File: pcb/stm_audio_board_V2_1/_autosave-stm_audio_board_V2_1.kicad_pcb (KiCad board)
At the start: 4 copper layers, 66.1 x 71 mm, 147 parts, among them J1 Power conn, J2 STlink, J3 Audio_sig, J4 Conn_01x01_taptempo, J5 Conn_01x10_display, J6 Conn_01x03_pot_ext, J7 Conn_01x8_pots_internal, SW1 SW_SPST, U1 STM32H747IGTx, U2 OP275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

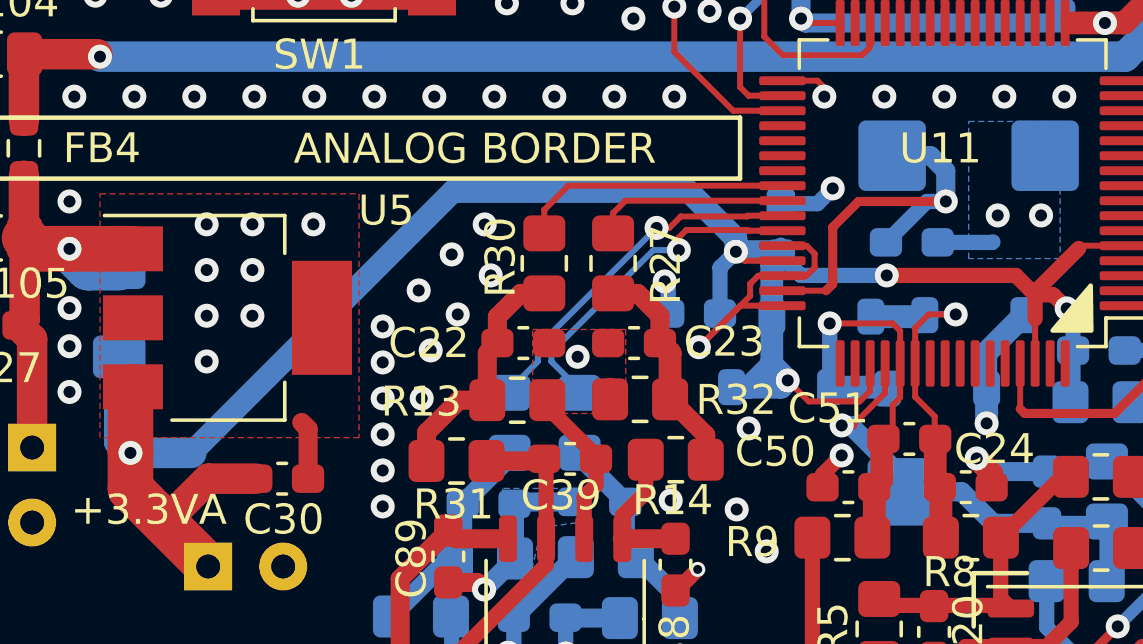
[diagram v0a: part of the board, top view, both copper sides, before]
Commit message: input stage is done, fixes for the audioboardV2_1 over
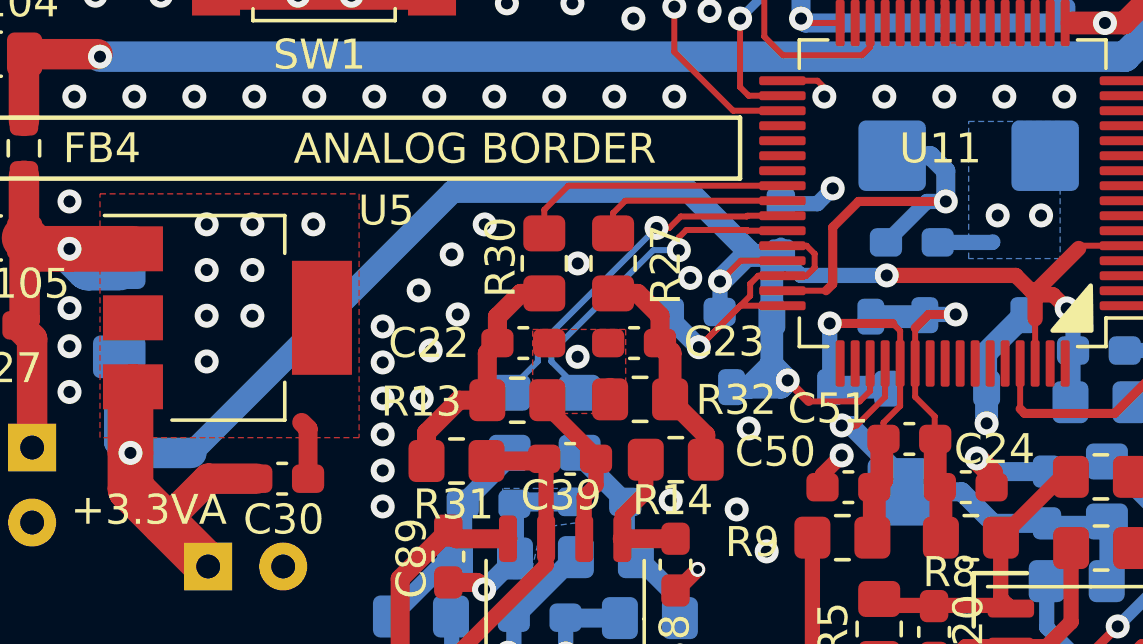
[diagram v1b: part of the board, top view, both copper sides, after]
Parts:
- moved C33 0.05 mm to (208.8, 97.9)
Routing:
- net +3.3VA: track 80.2 -> 82.1 mm
